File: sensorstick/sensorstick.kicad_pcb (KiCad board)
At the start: 2 copper layers, 38 x 26.8 mm, 16 parts, among them J1 U217-04XN-XXR84, U1 ESP32-C3_SUPERMINI, U2 SGP30, U3 SHT4x, U4 SCD40

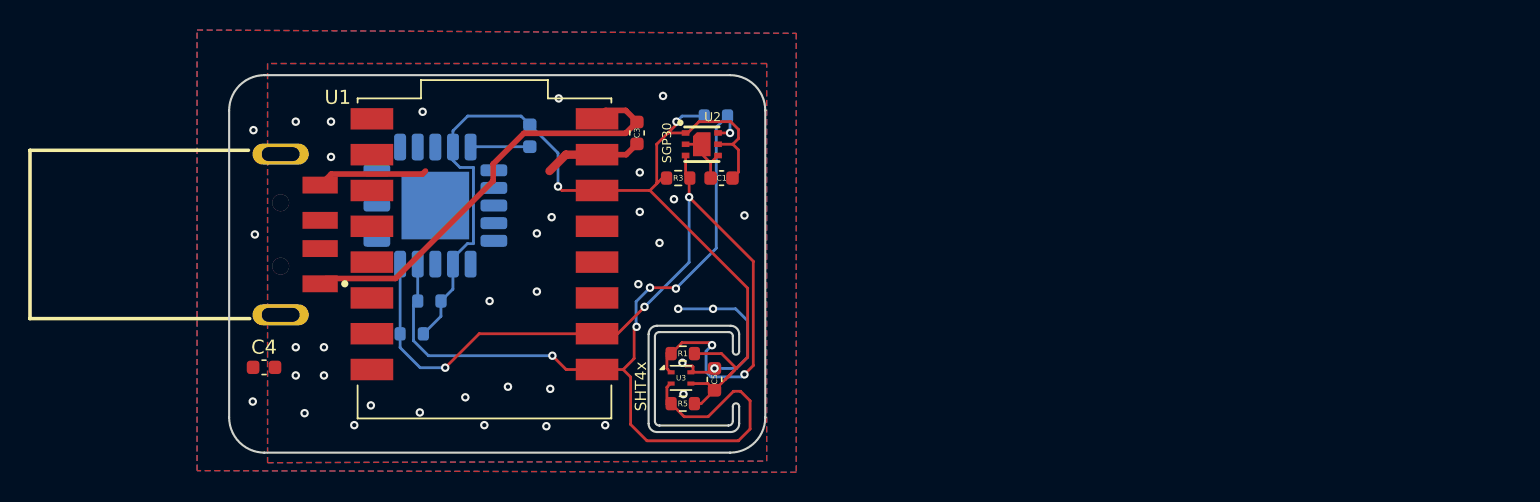
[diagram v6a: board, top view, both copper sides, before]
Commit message: moved all parts on the backside for easyer asambly
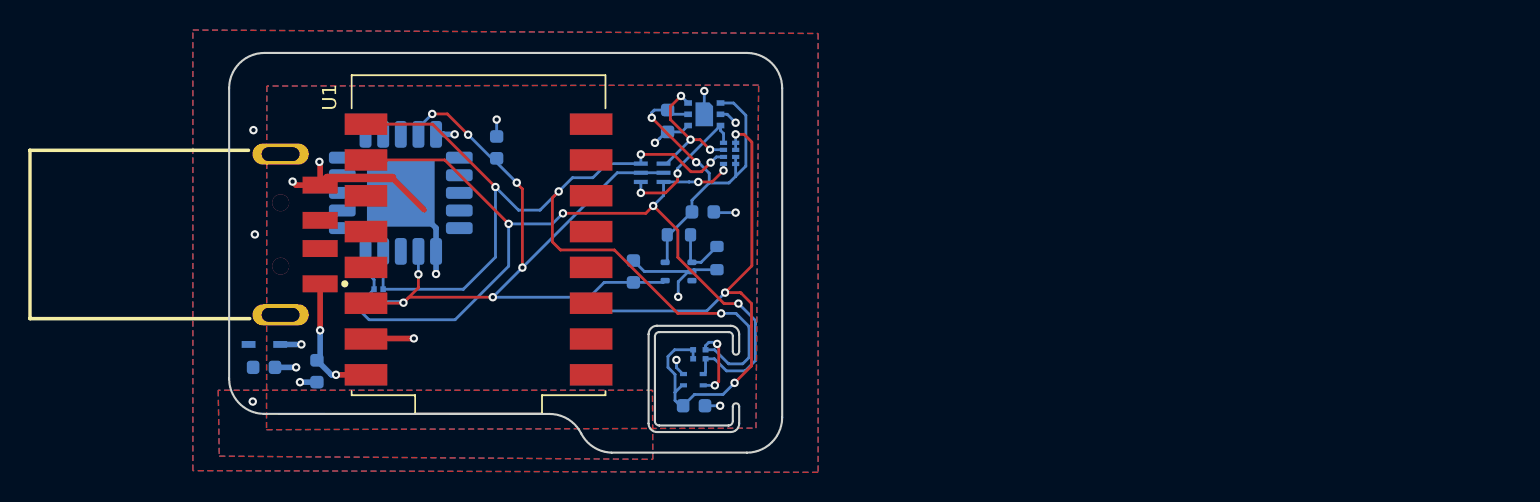
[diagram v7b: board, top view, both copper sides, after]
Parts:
- removed R1, R2, R3, R4, R5, R6: 10kΩ, Resistor_SMD:R_0603_1608Metric
- added C6: 0μF, Capacitor_SMD:C_0603_1608Metric, B.Cu at (92.9, 96.9)
- added C7: 100nF, Capacitor_SMD:C_0603_1608Metric, B.Cu at (88.0, 101.1)
- added D1: D5V0L1B2WS-7, easyeda2kicad:SOD-323_L1.8-W1.3-LS2.5-BI, B.Cu at (61.8, 106.3)
- added R7: 499kΩ, Resistor_SMD:R_0603_1608Metric, B.Cu at (91.2, 98.5)
- added R8: 1MΩ, Resistor_SMD:R_0603_1608Metric, B.Cu at (93.9, 100.2)
- added RN1: 2D02WGJ0103TCE, easyeda2kicad:RES-ARRAY-SMD_0402-4P-L1.0-W1.0-BL, B.Cu at (69.9, 102.8)
- added RN2: 2D02WGJ0103TCE, easyeda2kicad:RES-ARRAY-SMD_0402-4P-L1.0-W1.0-BL, B.Cu at (92.6, 107.0)
- added RN3: 4D02WGF1002TCE, easyeda2kicad:RES-ARRAY-SMD_0402-8P-L2.0-W1.0-BL, B.Cu at (94.8, 92.8)
- added U5: TPS71533__SC70, Package_TO_SOT_SMD:SOT-353_SC-70-5, B.Cu at (91.2, 101.1)
- added U6: 2N7002DW, 2N7002DW:SOT363, B.Cu at (89.3, 94.1)
- C1, C3, C4, C5, U2, U3: moved to B.Cu
- U4: value SCD40 -> SCD40-D-R2
- moved C3 28.3 mm to (65.5, 108.2)
- moved C1 16.1 mm to (78.2, 92.3), turned to -90 degrees
- moved C2 9.83 mm to (90.4, 90.5)
- moved U4 2.61 mm to (71.5, 95.5)
- moved C5 2.37 mm to (92.2, 110.7), turned to 0 degrees
- moved U2 2.13 mm to (93.0, 90.0), turned to 180 degrees
- moved U1 1.70 mm to (77.0, 98.6), turned to 180 degrees
- moved U3 0.88 mm to (92.2, 108.8), turned to 180 degrees
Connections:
- C2 pad 1: +3.3V -> +1.8V
- U1 pad 0: /I2C_SCL -> /I2C_SCL_3.3
- U1 pad 1: /IC2_SDA -> /IC2_SDA_3.3
- U2 pad 1: +3.3V -> +1.8V
- U2 pad 3: /IC2_SDA -> /IC2_SDA_1.8
- U2 pad 5: +3.3V -> +1.8V
- U2 pad 6: /I2C_SCL -> /I2C_SCL_1.8
- U3 pad 1: /IC2_SDA -> /IC2_SDA_3.3
- U3 pad 2: /I2C_SCL -> /I2C_SCL_3.3
- U4 pad 10: /IC2_SDA -> /IC2_SDA_3.3
- U4 pad 9: /I2C_SCL -> /I2C_SCL_3.3
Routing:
- net /I2C_SCL_3.3: track 0.00 -> 78.7 mm, vias 0 -> 7
- net /I2C_SCL: track 70.2 -> 0.00 mm, vias 5 -> 0
- net /IC2_SDA_3.3: track 0.00 -> 70.0 mm, vias 0 -> 6
- net /IC2_SDA: track 62.8 -> 0.00 mm, vias 5 -> 0
- net +1.8V: track 0.00 -> 26.3 mm, vias 0 -> 2
- net +3.3V: track 80.5 -> 104.4 mm, vias 2 -> 10
- net +5V: track 30.8 -> 9.75 mm, vias 0 -> 2
- net /IC2_SDA_1.8: track 0.00 -> 10.3 mm, vias 0 -> 2
- net GND: track 37.3 -> 47.5 mm, vias 35 -> 16
- net /I2C_SCL_1.8: track 0.00 -> 10.1 mm, vias 0 -> 3
- net Net-(U5-FB): track 0.00 -> 4.23 mm
- added copper zone on In1.Cu, net Earth
- added copper zone on In2.Cu, net Earth
- added copper zone on In1.Cu, net GND
- added copper zone on In2.Cu, net GND
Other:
- board size 38 x 26.8 mm -> 39.2 x 28.4 mm
- copper layers 2 -> 4

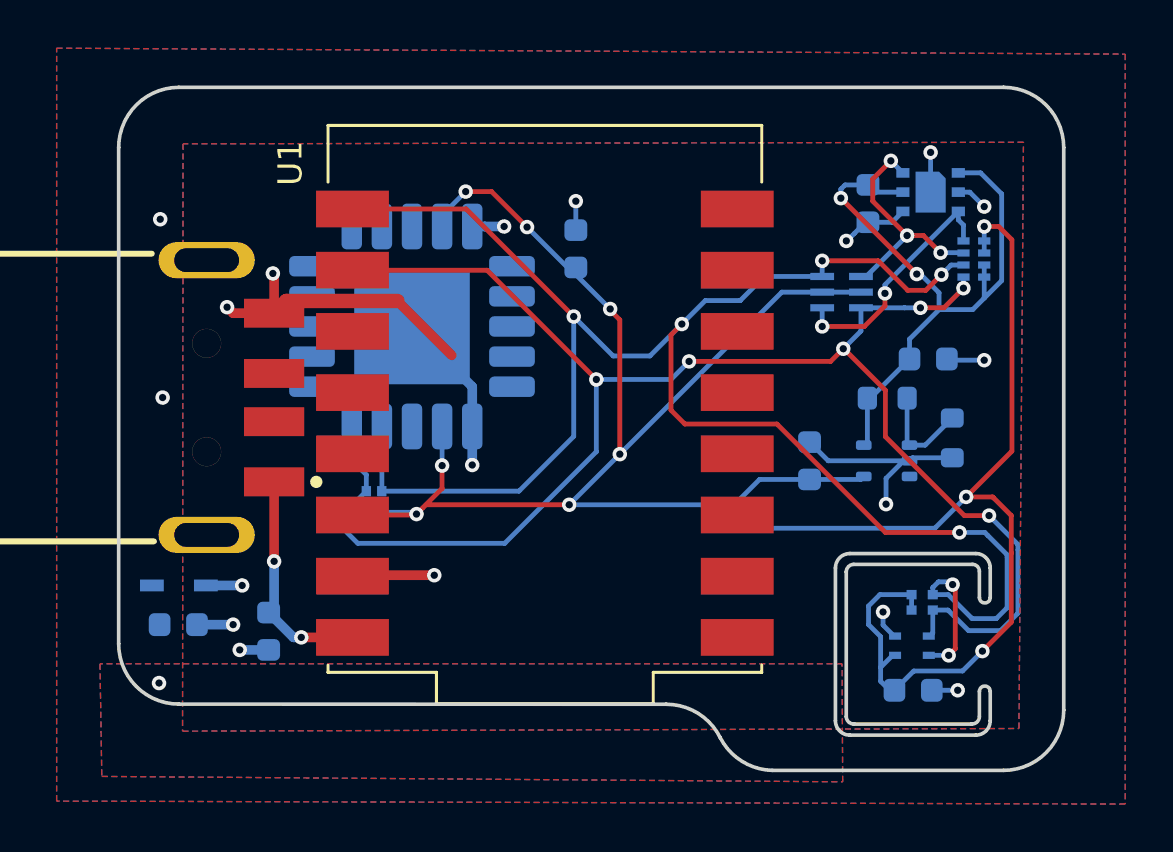
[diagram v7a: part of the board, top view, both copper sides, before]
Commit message: added more vias
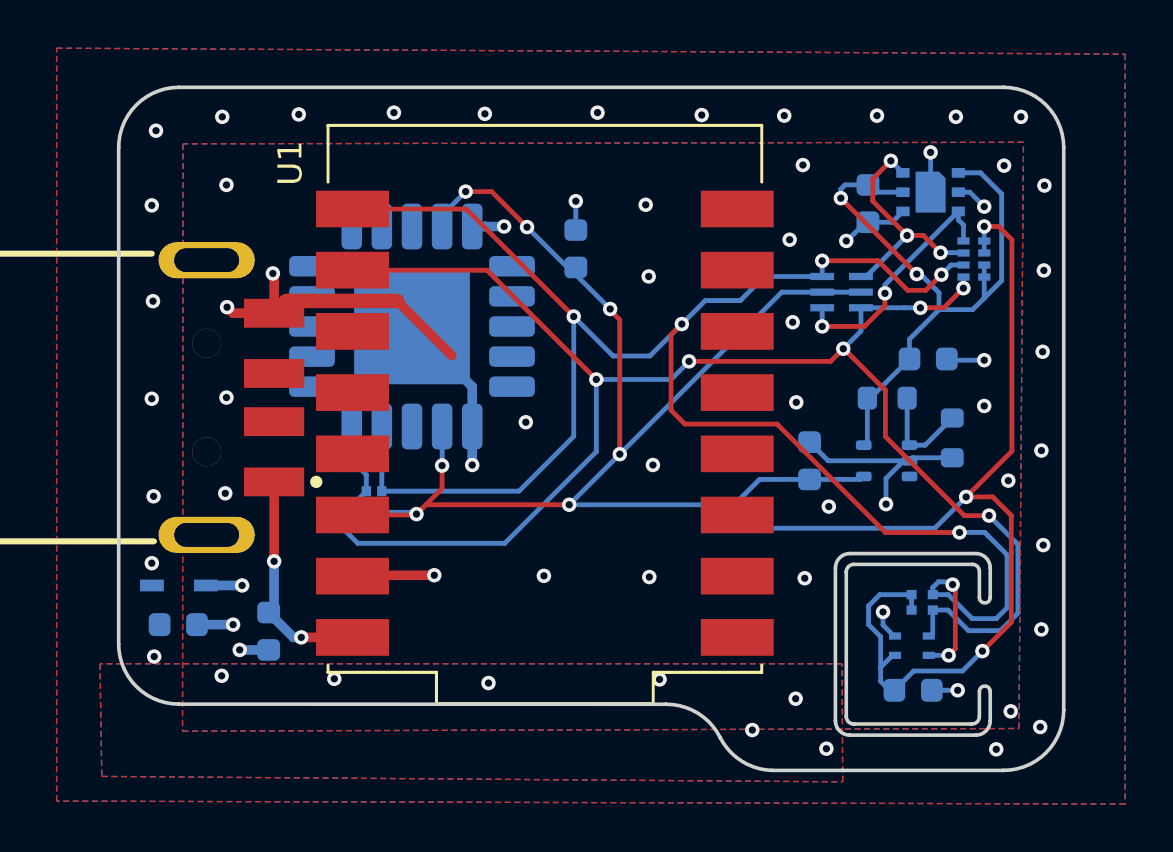
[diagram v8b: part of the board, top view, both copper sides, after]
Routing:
- net GND: vias 16 -> 35
- net Earth: vias 3 -> 32
